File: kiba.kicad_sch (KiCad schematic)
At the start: 18 parts, among them J1 Raspberry_Pi_2_3, Q1 2N7002NXAKR, U1 LM1117MP-3.3

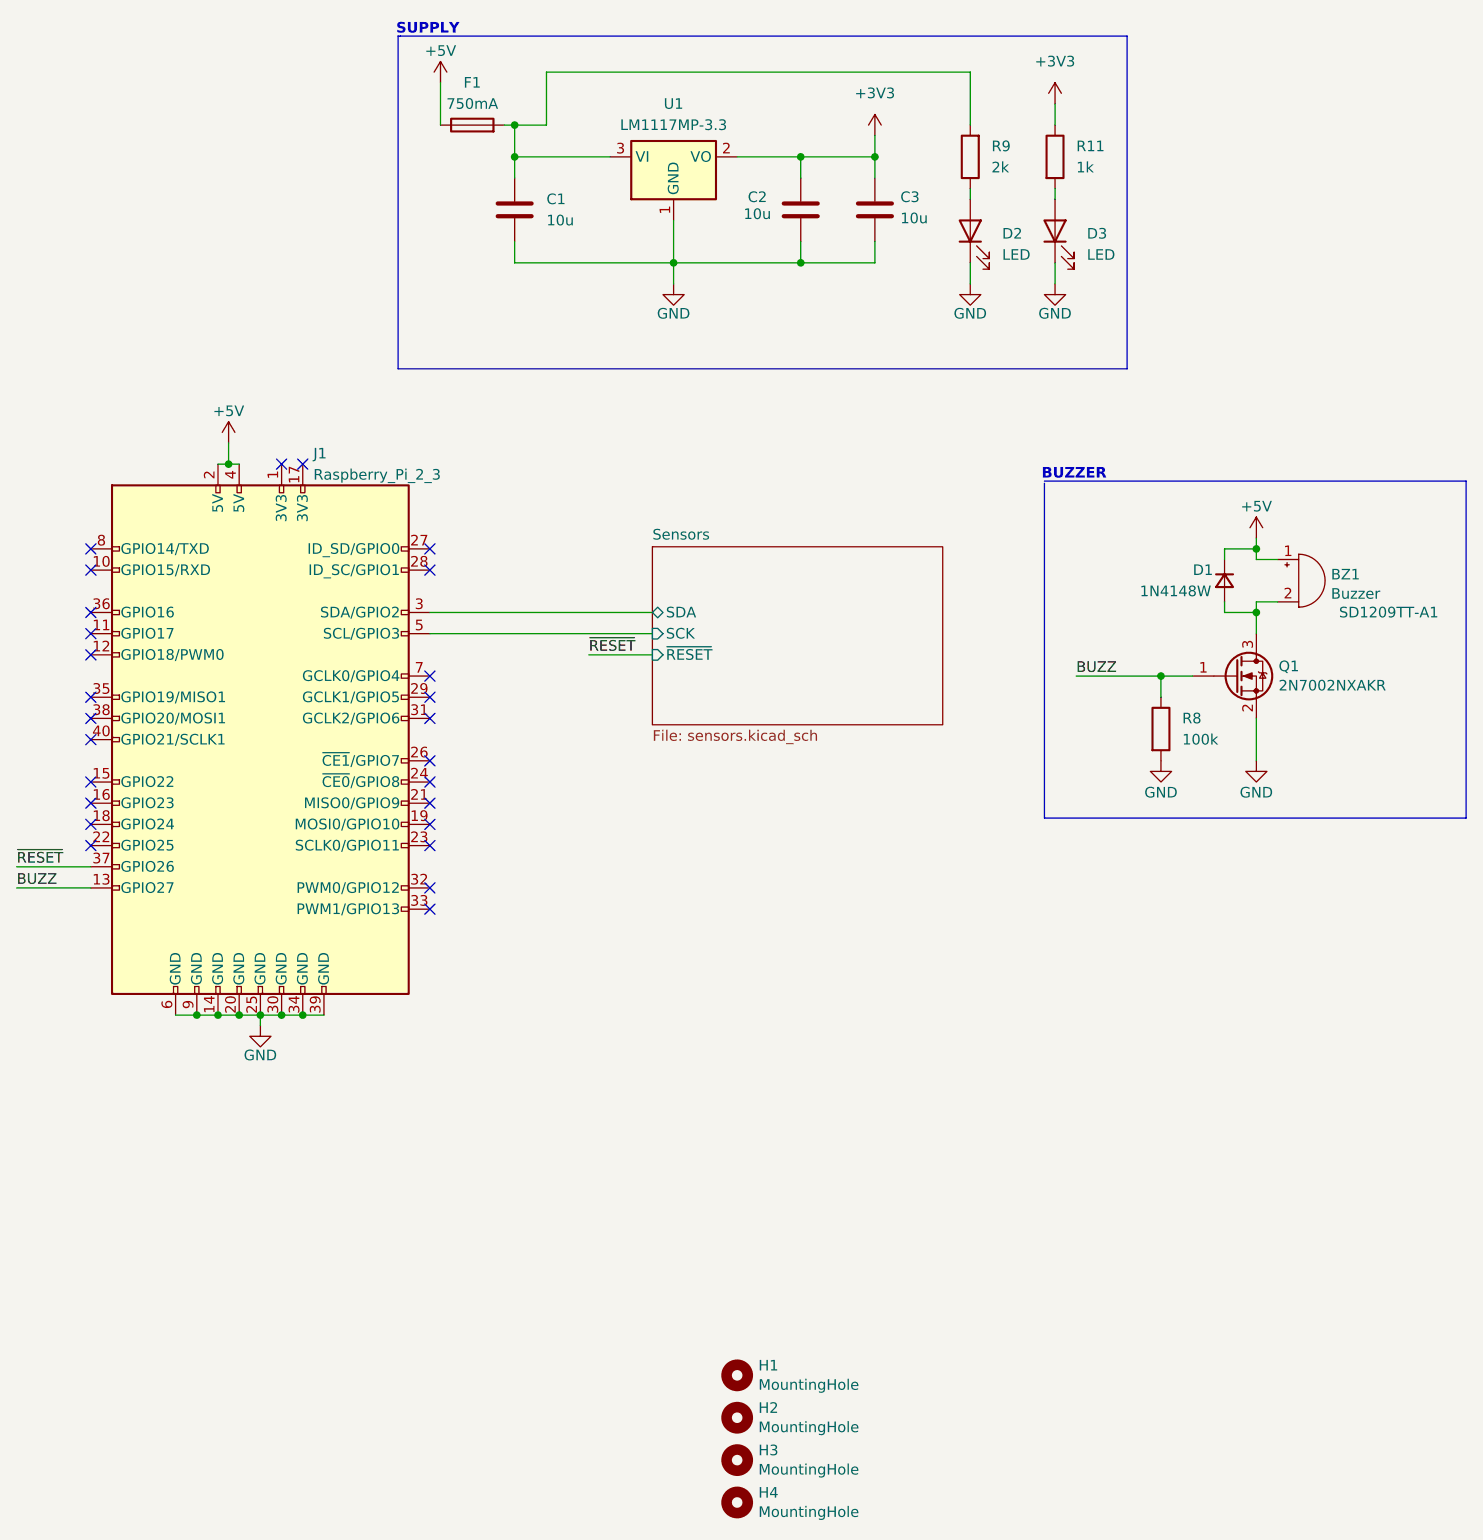
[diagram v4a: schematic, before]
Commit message: production files for jlcpcb, added passives for DNP sensors
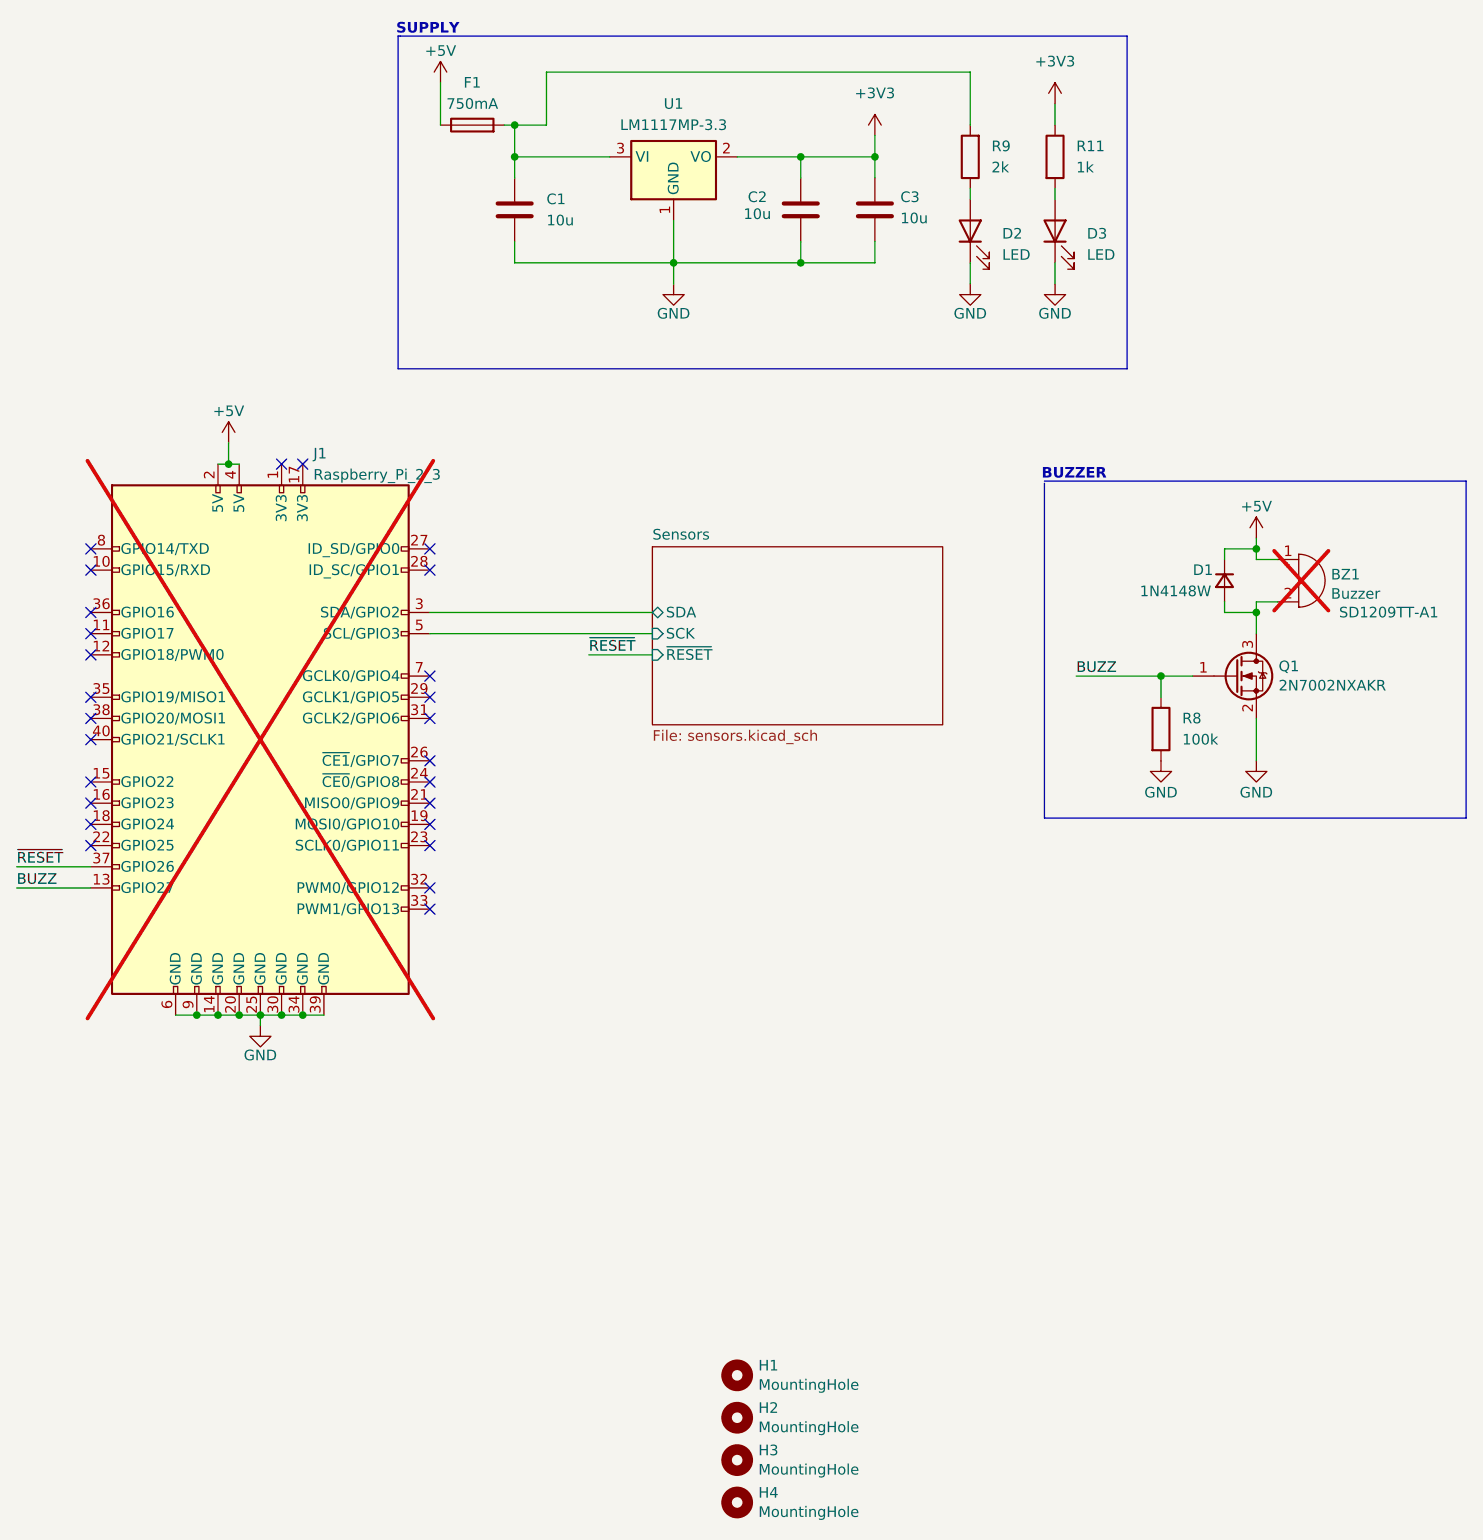
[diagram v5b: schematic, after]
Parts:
- BZ1, J1: now not fitted; now left out of the parts list
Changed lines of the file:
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@@
 		(on_board yes)
 		(dnp no)
-		(property "Reference" "#PWR25"
+		(property "Reference" "#PWR025"
 			(at 214.63 111.76 0)
 			(effects
@@
 			(project "kiba"
 				(path "/830d4d2d-479f-4d6d-bef5-9f1041d3fb90"
-					(reference "#PWR25")
+					(reference "#PWR025")
 					(unit 1)
 				)
@@
 		(on_board yes)
 		(dnp no)
-		(property "Reference" "#PWR71"
+		(property "Reference" "#PWR071"
 			(at 180.34 54.61 0)
 			(effects
@@
 			(project "kiba"
 				(path "/830d4d2d-479f-4d6d-bef5-9f1041d3fb90"
-					(reference "#PWR71")
+					(reference "#PWR071")
 					(unit 1)
 				)
@@
 		(on_board yes)
 		(dnp no)
-		(property "Reference" "#PWR72"
+		(property "Reference" "#PWR072"
 			(at 190.5 54.61 0)
 			(effects
@@
 			(project "kiba"
 				(path "/830d4d2d-479f-4d6d-bef5-9f1041d3fb90"
-					(reference "#PWR72")
+					(reference "#PWR072")
 					(unit 1)
 				)
@@
 		(unit 1)
 		(exclude_from_sim no)
-		(in_bom yes)
-		(on_board yes)
-		(dnp no)
+		(in_bom no)
+		(on_board yes)
+		(dnp yes)
 		(property "Reference" "BZ1"
 			(at 223.5708 83.0834 0)
@@
 		(on_board yes)
 		(dnp no)
-		(property "Reference" "#PWR26"
+		(property "Reference" "#PWR026"
 			(at 95.25 143.51 0)
 			(effects
@@
 			(project "kiba"
 				(path "/830d4d2d-479f-4d6d-bef5-9f1041d3fb90"
-					(reference "#PWR26")
+					(reference "#PWR026")
 					(unit 1)
 				)
@@
 		(dnp no)
 		(fields_autoplaced yes)
-		(property "Reference" "#PWR70"
+		(property "Reference" "#PWR070"
 			(at 190.5 30.48 0)
 			(effects
@@
 			(project ""
 				(path "/830d4d2d-479f-4d6d-bef5-9f1041d3fb90"
-					(reference "#PWR70")
+					(reference "#PWR070")
 					(unit 1)
 				)
@@
 		(dnp no)
 		(fields_autoplaced yes)
-		(property "Reference" "#PWR3"
+		(property "Reference" "#PWR03"
 			(at 168.91 34.29 0)
 			(effects
@@
 			(project "kiba"
 				(path "/830d4d2d-479f-4d6d-bef5-9f1041d3fb90"
-					(reference "#PWR3")
+					(reference "#PWR03")
 					(unit 1)
 				)
@@
 		(on_board yes)
 		(dnp no)
-		(property "Reference" "#PWR1"
+		(property "Reference" "#PWR01"
 			(at 91.44 71.12 0)
 			(effects
@@
 			(project "kiba"
 				(path "/830d4d2d-479f-4d6d-bef5-9f1041d3fb90"
-					(reference "#PWR1")
+					(reference "#PWR01")
 					(unit 1)
 				)
@@
 		(on_board yes)
 		(dnp no)
-		(property "Reference" "#PWR22"
+		(property "Reference" "#PWR022"
 			(at 116.84 27.94 0)
 			(effects
@@
 			(project "kiba"
 				(path "/830d4d2d-479f-4d6d-bef5-9f1041d3fb90"
-					(reference "#PWR22")
+					(reference "#PWR022")
 					(unit 1)
 				)
@@
 		(on_board yes)
 		(dnp no)
-		(property "Reference" "#PWR24"
+		(property "Reference" "#PWR024"
 			(at 214.63 82.55 0)
 			(effects
@@
 			(project "kiba"
 				(path "/830d4d2d-479f-4d6d-bef5-9f1041d3fb90"
-					(reference "#PWR24")
+					(reference "#PWR024")
 					(unit 1)
 				)
@@
 		(on_board yes)
 		(dnp no)
-		(property "Reference" "#PWR23"
+		(property "Reference" "#PWR023"
 			(at 203.2 111.76 0)
 			(effects
@@
 			(project "kiba"
 				(path "/830d4d2d-479f-4d6d-bef5-9f1041d3fb90"
-					(reference "#PWR23")
+					(reference "#PWR023")
 					(unit 1)
 				)
@@
 		(unit 1)
 		(exclude_from_sim no)
-		(in_bom yes)
-		(on_board yes)
-		(dnp no)
+		(in_bom no)
+		(on_board yes)
+		(dnp yes)
 		(property "Reference" "J1"
 			(at 101.6 68.58 0)
@@
 		(on_board yes)
 		(dnp no)
-		(property "Reference" "#PWR2"
+		(property "Reference" "#PWR02"
 			(at 144.78 54.61 0)
 			(effects
@@
 			(project "kiba"
 				(path "/830d4d2d-479f-4d6d-bef5-9f1041d3fb90"
-					(reference "#PWR2")
-					(unit 1)
-				)
+					(reference "#PWR02")
+					(unit 1)
+				)
